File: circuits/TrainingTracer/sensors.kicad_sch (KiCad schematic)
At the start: 25 parts, among them J2 BMX055/BNO055

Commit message: 回路完成
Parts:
- removed J2: BMX055/BNO055, symbol Connector_Generic:Conn_02x04_Counter_Clockwise
- added J11: BMX055/BNO055-1, Connector_PinSocket_2.54mm:PinSocket_1x04_P2.54mm_Vertical, symbol Connector_Generic:Conn_01x04
- added J12: BMX055/BNO055-2, Connector_PinSocket_2.54mm:PinSocket_1x04_P2.54mm_Vertical, symbol Connector_Generic:Conn_01x04
- JP1: footprint (none) -> Jumper:SolderJumper-3_P2.0mm_Open_TrianglePad1.0x1.5mm
- JP2: footprint (none) -> Jumper:SolderJumper-2_P1.3mm_Open_TrianglePad1.0x1.5mm
- R10, R12, R4, R8: value R_Small_US -> 33; footprint (none) -> Resistor_THT:R_Axial_DIN0204_L3.6mm_D1.6mm_P7.62mm_Horizontal
- R11, R14, R15, R6, R7, R9: value R_Small_US -> 1k; footprint (none) -> Resistor_THT:R_Axial_DIN0204_L3.6mm_D1.6mm_P7.62mm_Horizontal
- R13, R5: value R_Small_US -> 75; footprint (none) -> Resistor_THT:R_Axial_DIN0204_L3.6mm_D1.6mm_P7.62mm_Horizontal
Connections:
- net +3.3V: now also J11.1 (Pin_1)
- net GND: now also J11.2 (Pin_2)
- net SCL: now also J11.4 (Pin_4)
- net SDA: now also J11.3 (Pin_3)
- net at JP1.2 (C): now also J12.3 (Pin_3)
- net at JP2.1 (A): now also J12.1 (Pin_1)

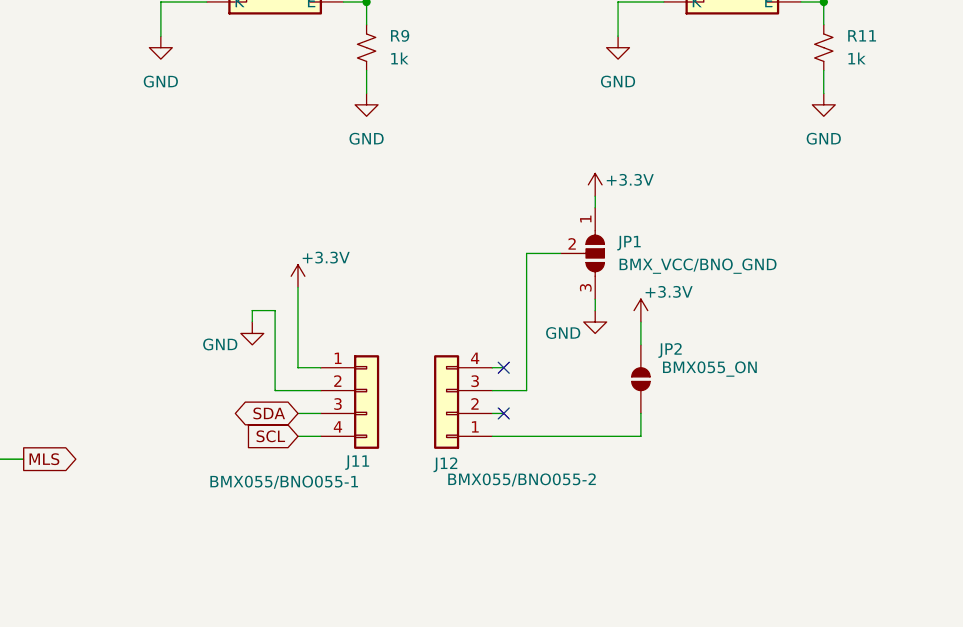
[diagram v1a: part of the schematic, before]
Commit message: PCBのPDF出力
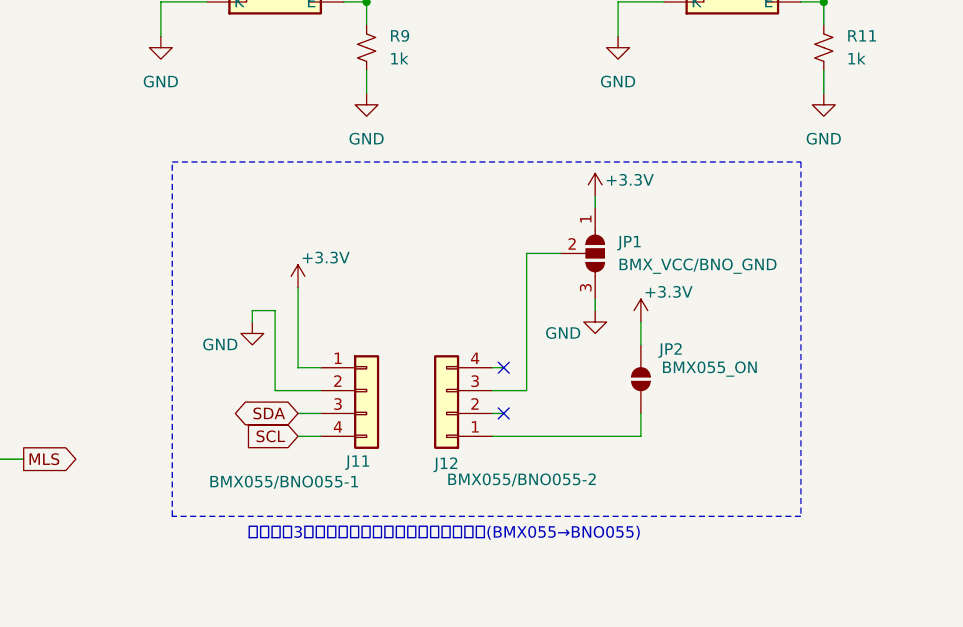
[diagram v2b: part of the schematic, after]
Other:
- note added: "改造箇所3：ディスコンセンサの置き換え対応(BMX055→BNO055)"
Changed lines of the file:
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@@
 	(generator_version "9.0")
 	(paper "A4")
+	(rectangle
+		(start 90.17 77.47)
+		(end 160.02 116.84)
+		(stroke
+			(width 0)
+			(type dash_dot)
+		)
+		(fill
+			(type none)
+		)
+	)
+	(text "改造箇所3：ディスコンセンサの置き換え対応(BMX055→BNO055)"
+		(exclude_from_sim no)
+		(at 120.396 118.872 0)
+		(effects
+			(font
+				(size 1.27 1.27)
+			)
+		)
+	)
 	(junction
 		(at 111.76 59.69)
